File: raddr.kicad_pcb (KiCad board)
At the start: 2 copper layers, 16 x 17.3 mm, 8 parts, among them J1 Conn_01x03, J2 Conn_01x01, J3 Conn_01x04, J4 Conn_01x01, U1 PMS150C-U06

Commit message: Delete a VIA.
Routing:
- net +5VD: track 16.2 -> 17.1 mm, vias 3 -> 2
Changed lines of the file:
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@@
 	)
 	(segment
-		(start 135.6542 106.368)
-		(end 135.6614 106.3752)
+		(start 135.6542 106.7316)
+		(end 135.974892 107.052292)
 		(width 0.4)
 		(layer "F.Cu")
@@
 	)
 	(segment
-		(start 143.2975 107.6625)
-		(end 143.552099 107.407901)
+		(start 135.6542 105.271)
+		(end 135.6542 106.7316)
 		(width 0.4)
 		(layer "F.Cu")
@@
 		(start 134.4676 109.7035)
 		(end 134.5666 109.8025)
-		(width 0.4)
-		(layer "F.Cu")
-		(net 2)
-	)
-	(segment
-		(start 135.6542 105.271)
-		(end 135.6542 106.368)
 		(width 0.4)
 		(layer "F.Cu")
@@
 	)
 	(via
-		(at 143.552099 107.407901)
-		(size 0.6)
-		(drill 0.3)
-		(layers "F.Cu" "B.Cu")
-		(net 2)
-	)
-	(via
-		(at 135.6614 106.3752)
+		(at 135.974892 107.052292)
 		(size 0.6)
 		(drill 0.3)
@@
 	)
 	(segment
-		(start 135.6614 107.3658)
-		(end 135.89 107.3658)
+		(start 144.28 107.0523)
+		(end 144.28 106.68)
 		(width 0.4)
 		(layer "B.Cu")
@@
 	)
 	(segment
-		(start 143.210198 107.066)
-		(end 143.552099 107.407901)
+		(start 135.6614 107.3658)
+		(end 135.974892 107.052308)
 		(width 0.4)
 		(layer "B.Cu")
@@
 	)
 	(segment
-		(start 135.6614 106.3752)
-		(end 135.6614 107.3658)
+		(start 135.974892 107.052308)
+		(end 135.974892 107.052292)
 		(width 0.4)
 		(layer "B.Cu")
@@
 	)
 	(segment
-		(start 136.1898 107.066)
-		(end 143.210198 107.066)
+		(start 135.9749 107.0523)
+		(end 144.28 107.0523)
 		(width 0.4)
 		(layer "B.Cu")
@@
 	)
 	(segment
-		(start 135.89 107.3658)
-		(end 136.1898 107.066)
+		(start 135.6614 107.3658)
+		(end 135.9749 107.0523)
 		(width 0.4)
 		(layer "B.Cu")

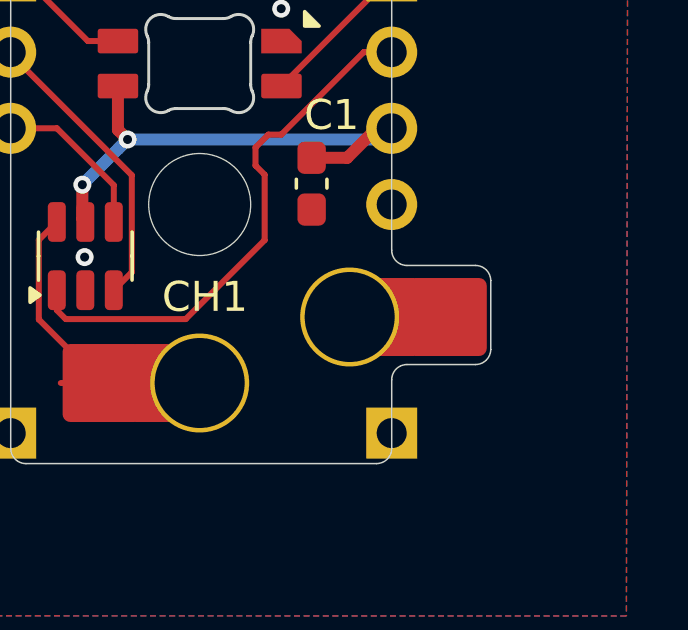
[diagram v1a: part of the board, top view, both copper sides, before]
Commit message: Increase distance of board perimeter to pad to eliminate warning.
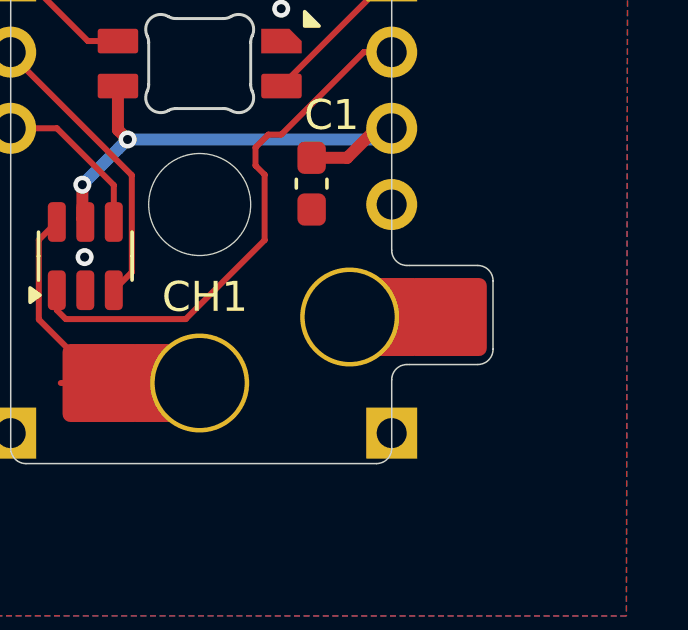
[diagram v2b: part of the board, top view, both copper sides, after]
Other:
- board size 16 x 17.3 mm -> 16.1 x 17.3 mm
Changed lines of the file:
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@@
 		(fp_arc
 			(start 1.699999 -0.702841)
-			(mid 1.712528 -0.814067)
+			(mid 1.712529 -0.814066)
 			(end 1.749484 -0.919719)
 			(stroke
@@
 		(fp_arc
 			(start 1.749484 0.919721)
-			(mid 1.712518 0.81407)
+			(mid 1.71251 0.814072)
 			(end 1.699999 0.702844)
 			(stroke
@@
 	)
 	(gr_arc
-		(start 147.574 111.252)
-		(mid 147.93321 111.40079)
-		(end 148.082 111.76)
+		(start 147.6502 111.252)
+		(mid 148.00941 111.40079)
+		(end 148.1582 111.76)
 		(stroke
 			(width 0.05)
@@
 	)
 	(gr_line
-		(start 147.574 114.554)
-		(end 145.288 114.554)
+		(start 145.288 111.252)
+		(end 145.3642 111.252)
+		(stroke
+			(width 0.05)
+			(type default)
+		)
+		(layer "Edge.Cuts")
+	)
+	(gr_line
+		(start 147.6502 114.554)
+		(end 145.3642 114.554)
 		(stroke
 			(width 0.05)
@@
 	)
 	(gr_arc
-		(start 148.082 114.046)
-		(mid 147.93321 114.40521)
-		(end 147.574 114.554)
+		(start 148.1582 114.046)
+		(mid 148.00941 114.40521)
+		(end 147.6502 114.554)
 		(stroke
 			(width 0.05)
@@
 	)
 	(gr_line
-		(start 145.288 111.252)
-		(end 147.574 111.252)
+		(start 145.3642 111.252)
+		(end 147.6502 111.252)
+		(stroke
+			(width 0.05)
+			(type default)
+		)
+		(layer "Edge.Cuts")
+	)
+	(gr_line
+		(start 145.288 114.554)
+		(end 145.3642 114.554)
 		(stroke
 			(width 0.05)
@@
 	)
 	(gr_line
-		(start 148.082 111.76)
-		(end 148.082 114.046)
-		(stroke
-			(width 0.05)
+		(start 148.1582 111.76)
+		(end 148.1582 114.046)
+		(stroke
+			(width 0.05)

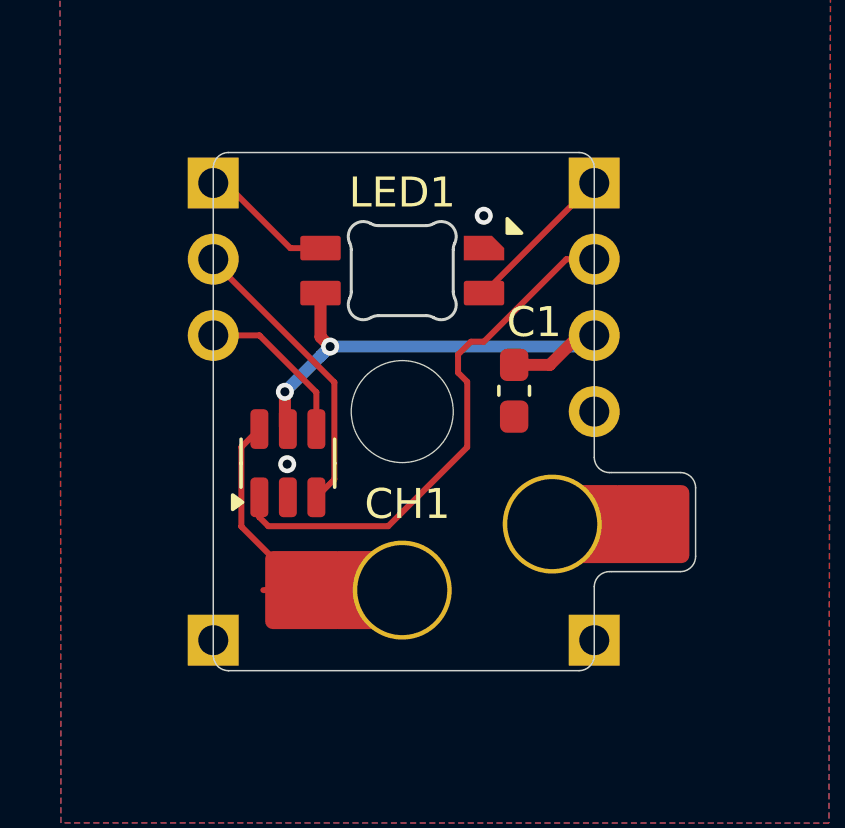
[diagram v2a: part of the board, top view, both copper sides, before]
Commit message: Fix thermal relieve issues by rotating spokes for pins near board edge.
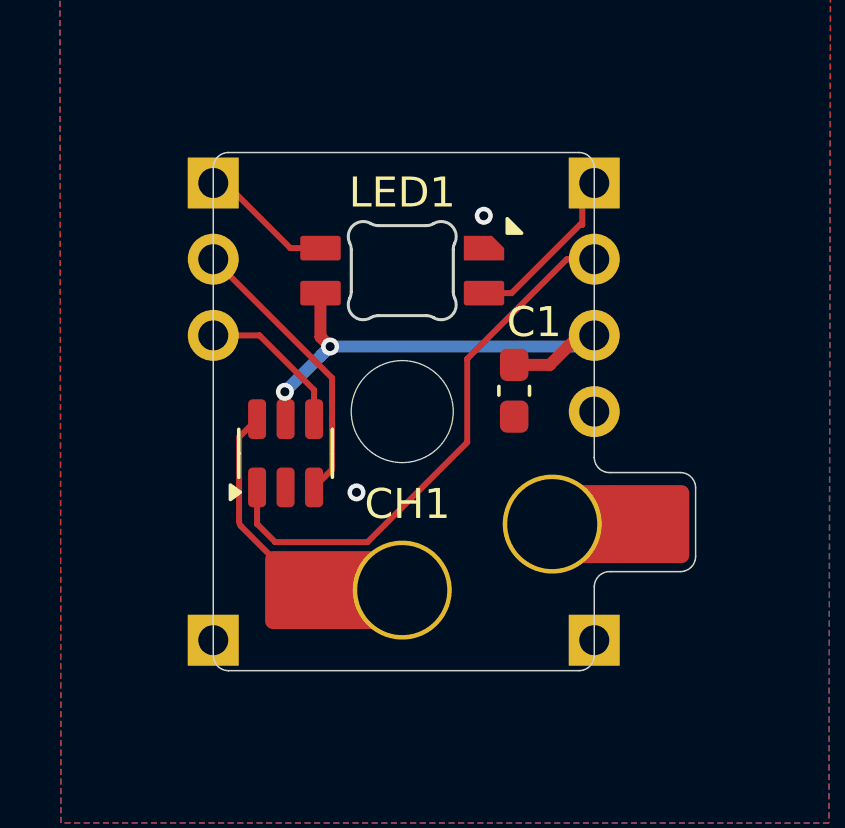
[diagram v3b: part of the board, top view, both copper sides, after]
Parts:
- moved U1 0.34 mm to (134.5, 110.6)
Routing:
- net GND: track 0.40 -> 1.99 mm
- net SWITCH: track 7.88 -> 6.84 mm
- net LED_DIN: track 5.03 -> 5.61 mm
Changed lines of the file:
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@@
 			(pinfunction "Pin_1")
 			(pintype "passive")
+			(thermal_bridge_angle 22.5)
 		)
 		(model "${KICAD8_3DMODEL_DIR}/Connector_PinSocket_2.54mm.3dshapes/PinSocket_1x01_P2.54mm_Vertical.wrl"
@@
 			(pinfunction "1")
 			(pintype "passive")
+			(thermal_bridge_angle 45)
 		)
 		(pad "1" smd roundrect
@@
 			(pinfunction "Pin_1")
 			(pintype "passive")
+			(thermal_bridge_angle -22.5)
 		)
 		(model "${KICAD8_3DMODEL_DIR}/Connector_PinSocket_2.54mm.3dshapes/PinSocket_1x01_P2.54mm_Vertical.wrl"
@@
 	(footprint "Package_TO_SOT_SMD:SOT-23-6"
 		(layer "F.Cu")
-		(at 134.5666 110.94 90)
+		(at 134.4904 110.6098 90)
 		(descr "SOT, 6 Pin (https://www.jedec.org/sites/default/files/docs/Mo-178c.PDF variant AB), generated with kicad-footprint-generator ipc_gullwing_generator.py")
 		(tags "SOT TO_SOT_SMD")
@@
 			(pinfunction "Pin_4")
 			(pintype "passive")
+			(thermal_bridge_angle 45)
 		)
 		(model "${KICAD8_3DMODEL_DIR}/Connector_PinSocket_2.54mm.3dshapes/PinSocket_1x04_P2.54mm_Vertical.wrl"
@@
 	)
 	(segment
+		(start 132.635718 116.284282)
+		(end 132.6388 116.276842)
+		(width 0.508)
+		(layer "F.Cu")
+		(net 1)
+	)
+	(segment
 		(start 132.48 116.44)
 		(end 132.48 116.84)
@@
 		(net 1)
 	)
+	(segment
+		(start 132.08 116.84)
+		(end 132.635718 116.284282)
+		(width 0.508)
+		(layer "F.Cu")
+		(net 1)
+	)
+	(segment
+		(start 134.493 111.753576)
+		(end 134.4904 111.7473)
+		(width 0.508)
+		(layer "F.Cu")
+		(net 1)
+	)
 	(via
-		(at 134.5438 110.9726)
+		(at 136.8552 111.9124)
 		(size 0.6)
 		(drill 0.3)
@@
 	)
 	(segment
+		(start 132.08 116.84)
+		(end 132.6388 116.2812)
+		(width 0.508)
+		(layer "B.Cu")
+		(net 1)
+	)
+	(segment
+		(start 134.4676 108.5596)
+		(end 134.4676 109.4495)
+		(width 0.4)
+		(layer "F.Cu")
+		(net 2)
+	)
+	(segment
 		(start 135.6542 106.7316)
 		(end 135.974892 107.052292)
@@
 	)
 	(segment
-		(start 134.4676 109.7035)
-		(end 134.5666 109.8025)
-		(width 0.4)
-		(layer "F.Cu")
-		(net 2)
-	)
-	(segment
-		(start 134.4676 108.5596)
-		(end 134.4676 109.7035)
+		(start 134.4676 109.4495)
+		(end 134.4904 109.4723)
 		(width 0.4)
 		(layer "F.Cu")
@@
 	)
 	(segment
-		(start 134.4422 108.5342)
-		(end 134.4676 108.5596)
-		(width 0.4)
-		(layer "B.Cu")
-		(net 2)
-	)
-	(segment
 		(start 135.9749 107.0523)
 		(end 144.28 107.0523)
@@
 	)
 	(segment
-		(start 135.5166 112.0775)
-		(end 136.1166 111.4775)
+		(start 135.4404 111.7473)
+		(end 136.0404 111.1473)
 		(width 0.2)
 		(layer "F.Cu")
@@
 	)
 	(segment
-		(start 136.1166 108.243778)
-		(end 132.48 104.607178)
+		(start 136.0404 108.1004)
+		(end 132.08 104.14)
 		(width 0.2)
 		(layer "F.Cu")
@@
 	)
 	(segment
-		(start 136.1166 111.4775)
-		(end 136.1166 108.243778)
+		(start 136.0404 111.1473)
+		(end 136.0404 108.1004)
 		(width 0.2)
 		(layer "F.Cu")
@@
 	)
 	(segment
-		(start 135.5166 108.576224)
+		(start 135.4404 109.4723)
+		(end 135.4404 108.500024)
+		(width 0.2)
+		(layer "F.Cu")
+		(net 5)
+	)
+	(segment
+		(start 135.4404 108.500024)
 		(end 133.620376 106.68)
 		(width 0.2)
@@
 	)
 	(segment
-		(start 135.5166 109.8025)
-		(end 135.5166 108.576224)
+		(start 141.1042 105.271)
+		(end 142.022654 105.271)
 		(width 0.2)
 		(layer "F.Cu")
-		(net 5)
-	)
-	(segment
-		(start 141.1042 105.271)
-		(end 144.38 101.9952)
-		(width 0.2)
-		(layer "F.Cu")
 		(net 6)
 	)
 	(segment
-		(start 144.38 101.9952)
+		(start 144.38 102.99)
 		(end 144.38 101.6)
 		(width 0.2)
@@
 	)
 	(segment
-		(start 140.5448 110.4072)
-		(end 140.5448 108.226976)
+		(start 142.022654 105.271)
+		(end 144.303654 102.99)
 		(width 0.2)
 		(layer "F.Cu")
+		(net 6)
+	)
+	(segment
+		(start 144.303654 102.99)
+		(end 144.38 102.99)
+		(width 0.2)
+		(layer "F.Cu")
+		(net 6)
+	)
+	(segment
+		(start 134.144 113.57)
+		(end 137.221483 113.57)
+		(width 0.2)
+		(layer "F.Cu")
 		(net 7)
 	)
 	(segment
-		(start 140.667624 106.8898)
-		(end 141.099424 106.8898)
+		(start 140.5448 110.246683)
+		(end 140.5448 107.4608)
 		(width 0.2)
 		(layer "F.Cu")
@@
 	)
 	(segment
-		(start 140.5448 108.226976)
-		(end 140.24 107.922176)
+		(start 140.5448 107.4608)
+		(end 143.8656 104.14)
 		(width 0.2)
 		(layer "F.Cu")
@@
 	)
 	(segment
-		(start 140.24 107.317424)
-		(end 140.667624 106.8898)
+		(start 133.5404 111.7473)
+		(end 133.5404 112.9664)
 		(width 0.2)
 		(layer "F.Cu")
@@
 	)
 	(segment
-		(start 143.849224 104.14)
+		(start 133.5404 112.9664)
+		(end 134.144 113.57)
+		(width 0.2)
+		(layer "F.Cu")
+		(net 7)
+	)
+	(segment
+		(start 143.8656 104.14)
 		(end 144.38 104.14)
 		(width 0.2)
@@
 	)
 	(segment
-		(start 133.916601 113.04)
-		(end 137.912 113.04)
-		(width 0.2)
-		(layer "F.Cu")
-		(net 7)
-	)
-	(segment
-		(start 141.099424 106.8898)
-		(end 143.849224 104.14)
-		(width 0.2)
-		(layer "F.Cu")
-		(net 7)
-	)
-	(segment
-		(start 137.912 113.04)
-		(end 140.5448 110.4072)
-		(width 0.2)
-		(layer "F.Cu")
-		(net 7)
-	)
-	(segment
-		(start 140.24 107.922176)
-		(end 140.24 107.317424)
-		(width 0.2)
-		(layer "F.Cu")
-		(net 7)
-	)
-	(segment
-		(start 133.6166 112.739999)
-		(end 133.916601 113.04)
-		(width 0.2)
-		(layer "F.Cu")
-		(net 7)
-	)
-	(segment
-		(start 133.6166 112.0775)
-		(end 133.6166 112.739999)
+		(start 137.221483 113.57)
+		(end 140.5448 110.246683)
 		(width 0.2)
 		(layer "F.Cu")
@@
 	)
 	(segment
-		(start 133.0166 110.4025)
+		(start 132.9404 110.0723)
+		(end 132.9404 112.868437)
+		(width 0.2)
+		(layer "F.Cu")
+		(net 8)
+	)
+	(segment
+		(start 133.5404 109.4723)
+		(end 132.9404 110.0723)
+		(width 0.2)
+		(layer "F.Cu")
+		(net 8)
+	)
+	(arc
+		(start 132.9404 112.868437)
+		(mid 132.960204 112.967997)
 		(end 133.0166 113.0524)
 		(width 0.2)
 		(layer "F.Cu")
-		(net 8)
-	)
-	(segment
-		(start 133.6166 109.8025)
-		(end 133.0166 110.4025)
-		(width 0.2)
-		(layer "F.Cu")
-		(net 8)
-	)
-	(segment
-		(start 135.1342 115.17)
-		(end 133.75 115.17)
-		(width 0.2)
-		(layer "F.Cu")

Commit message: Redesign
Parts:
- removed J1: Conn_01x03, Connector_PinSocket_2.54mm:PinSocket_1x03_P2.54mm_Vertical
- removed J2, J4: Conn_01x01, Connector_PinSocket_2.54mm:PinSocket_1x01_P2.54mm_Vertical
- removed J3: Conn_01x04, Connector_PinSocket_2.54mm:PinSocket_1x04_P2.54mm_Vertical
- added DBG1: Conn_01x04, Connector_PinSocket_2.54mm:PinSocket_1x04_P2.54mm_Vertical, F.Cu at (-2.54, 19.1)
- added IN1: Conn_01x04, Connector_PinSocket_2.54mm:PinSocket_1x04_P2.54mm_Vertical, F.Cu at (-2.54, 0.00)
- added OUT1: Conn_01x04, Connector_PinSocket_2.54mm:PinSocket_1x04_P2.54mm_Vertical, F.Cu at (20.3, 0.00)
- CH1: value choc_v1_SW_HS -> KS33_SW_HS; footprint PCM_marbastlib-choc:SW_choc_v1_HS_CPG135001S30_1u -> PCM_marbastlib-xp-gateron_lp:SW_KS33_HS_KS-2P02B01-02_HS_1u
- U1: value PMS150C-U06 -> PY32F002AL1xS; footprint Package_TO_SOT_SMD:SOT-23-6 -> Package_SO:SOP-8_3.9x4.9mm_P1.27mm
- moved LED1 166.5 mm to (8.89, -0.08), turned to 180 degrees
- moved CH1 166.2 mm to (8.89, 5.08)
- moved C1 158.0 mm to (16.3, 13.0), turned to 0 degrees
- moved U1 151.0 mm to (16.2, 16.7), turned to 0 degrees
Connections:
- CH1 pad 1: GND -> SWITCH
- CH1 pad 2: SWITCH -> GND
- U1 pad 1: KEY_DIN -> +5VD
- U1 pad 2: GND -> KEY_DOUT
- U1 pad 3: KEY_DOUT -> KEY_DIN
- U1 pad 4: PROG_VPP -> SWC
- U1 pad 5: +5VD -> SWD
- U1 pad 6: SWITCH -> unconnected-(U1-PA2/PF2/NRST-Pad6)
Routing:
- net SWD: track 0.00 -> 21.5 mm
- net SWC: track 0.00 -> 18.5 mm
- net +5VD: track 16.7 -> 4.93 mm
- net KEY_DIN: track 17.8 -> 27.4 mm, vias 0 -> 1
- net KEY_DOUT: track 9.96 -> 17.5 mm, vias 0 -> 1
- net LED_DOUT: track 4.07 -> 9.94 mm, vias 0 -> 1
- net PROG_VPP: track 4.69 -> 0.00 mm
- net LED_DIN: track 5.61 -> 9.05 mm, vias 0 -> 1
- net SWITCH: track 6.84 -> 9.41 mm
- net GND: track 1.99 -> 0.00 mm, vias 2 -> 0
- added copper zone on F.Cu, net +5VD
- removed copper zone on B.Cu, net GND
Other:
- board size 16.1 x 17.3 mm -> 25.4 x 25.4 mm
- board text added: "GND"
- board text added: "KEY"
- board text added: "LED"
- board text added: "SWC"
- board text added: "SWD"
- board text added: "VCC"
